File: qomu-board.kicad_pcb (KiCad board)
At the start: 4 copper layers, 13 x 9.4 mm, 55 parts, among them SW2 Captouch Pads, U1 LDO-X2SON-1.2V, U10 RGB-LED, U2 LDO-X2SON-3.3V, U3 LDO-X2SON-2.5V, U4 SPI Flash, U5 ICE40UP5K-UWG30, U7 Crystal Oscillator, U9 USB-B

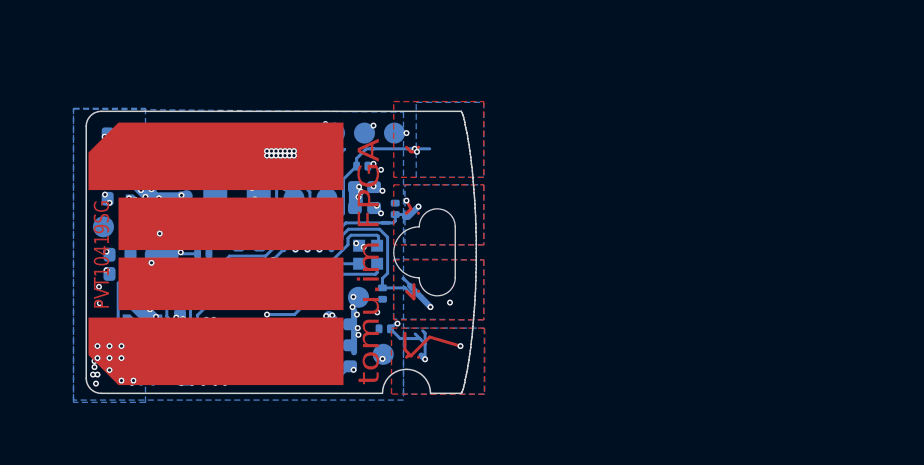
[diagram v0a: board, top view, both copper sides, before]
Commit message: Schematic/PCB cleanup
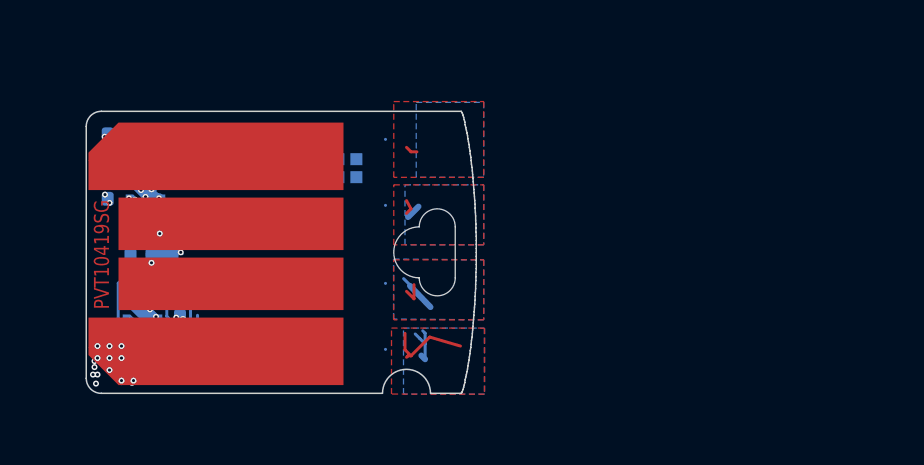
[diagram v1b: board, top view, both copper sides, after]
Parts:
- removed C10, C17, C24, C25, C5, C8: 0201, 1uF, 10V, X5R, 20%, qomu-board:C_0201_0603Metric
- removed C11, C20, C21, C23, C28, C4, C7: 0201, 100nF, 10V, X5R, 20%, qomu-board:C_0201_0603Metric
- removed C22: 0402, 10uF, 6.3V, X5R, 20%, qomu-board:C_0402_1005Metric
- removed D1, D2, D3, D4, D6: D5V0L1B2LP3-7, qomu-board:X1-DFN1006-2
- removed D5: VCUT05E1-SD0, qomu-board:TVS-11V
- removed R1, R5: 0201, 10k, 1/16W, qomu-board:R_0201_0603Metric
- removed R10: 0201, 100ohm, 1/16W, 1%, qomu-board:R_0201_0603Metric
- removed TP1, TP10, TP11, TP12, TP2, TP3, TP4, TP5, TP6, TP7, TP8, TP9: Testpoint, qomu-board:testpoint
- removed U4: SPI Flash, qomu-board:SON50P300X200X60-9N
- removed U5: ICE40UP5K-UWG30, qomu-board:iCE40UP5K-UWG30
- removed U7: Crystal Oscillator, qomu-board:XTAL-2520
- SW2: moved to B.Cu
- moved U10 2.97 mm to (25.7, 19.0), turned to 0 degrees
- moved SW2 1.13 mm to (27.0, 21.5), turned to 0 degrees
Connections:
- R11 pad 1: /ICE_USBN -> Net-(R11-Pad1)
- R12 pad 1: /ICE_USBP -> Net-(R12-Pad1)
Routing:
- net /SPI_MISO: track 29.6 -> 0.00 mm, vias 5 -> 0
- net /SPI_MOSI: track 27.6 -> 0.00 mm, vias 5 -> 0
- net /SPI_CS: track 22.7 -> 0.00 mm, vias 6 -> 0
- net /SPI_CLK: track 20.2 -> 0.00 mm, vias 3 -> 0
- net /CRESET: track 16.0 -> 0.00 mm, vias 4 -> 0
- net /SPI_IO2: track 15.1 -> 0.00 mm, vias 4 -> 0
- net +1V2: track 14.7 -> 1.24 mm, vias 18 -> 4
- net /SPI_IO3: track 9.91 -> 0.00 mm, vias 4 -> 0
- net /ICE_USBN: track 9.19 -> 0.00 mm
- net /ICE_USBP: track 9.01 -> 0.00 mm
- net +3V3: track 9.26 -> 0.86 mm, vias 44 -> 9
- net /TOUCH_1: track 13.0 -> 4.62 mm, vias 7 -> 0
- net +2V5: track 7.56 -> 0.02 mm, vias 10 -> 0
- net GND: track 20.1 -> 13.0 mm, vias 86 -> 25
- net /PU_CTRL_USBP: track 7.46 -> 0.74 mm, vias 2 -> 1
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- removed copper zone on In1.Cu, net +1V2
- removed copper zone on In2.Cu, net +1V2
- removed copper zone on In1.Cu, net +2V5
- removed copper zone on In1.Cu, net +3V3
- removed copper zone on In2.Cu, net +3V3
- removed copper zone on B.Cu, net +5V
- removed copper zone on In1.Cu, net +5V
- removed copper zone on In2.Cu, net +5V
- removed copper zone on In1.Cu, net /VCCPLL
- removed copper zone on B.Cu, net GND
- removed copper zone on In1.Cu, net GND
- removed copper zone on In2.Cu, net GND
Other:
- board text removed: "tomu.im FPGA"

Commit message: Added EOS-S3 and flash memory to schematics
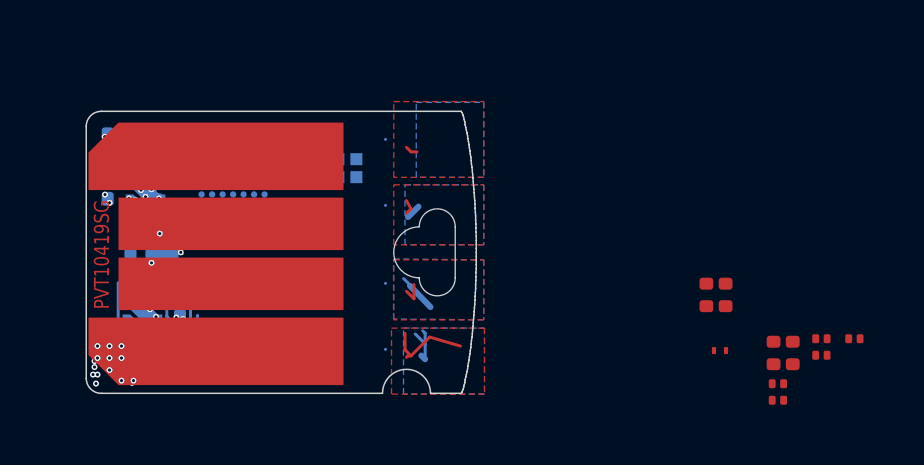
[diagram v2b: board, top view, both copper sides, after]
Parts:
- added C10: 1u/10V, qomu-board:C_0201_0603Metric, F.Cu at (40.3, 24.8)
- added C8: 1u/10V, qomu-board:C_0201_0603Metric, F.Cu at (40.3, 25.5)
- added D1: D5V0L1B2LP3-7, qomu-board:X1-DFN1006-2, F.Cu at (41.5, 24.7)
- added D2: D5V0L1B2LP3-7, qomu-board:X1-DFN1006-2, F.Cu at (40.1, 26.2)
- added D3: D5V0L1B2LP3-7, qomu-board:X1-DFN1006-2, F.Cu at (41.5, 25.2)
- added D4: D5V0L1B2LP3-7, qomu-board:X1-DFN1006-2, F.Cu at (40.1, 26.7)
- added D5: VCUT05E1-SD0, qomu-board:TVS-11V, F.Cu at (38.1, 25.1)
- added D6: D5V0L1B2LP3-7, qomu-board:X1-DFN1006-2, F.Cu at (42.6, 24.7)
- added IC1: EOS-S3, qomu-board:42-WLCSP, B.Cu at (21.9, 19.0)
- added R1: 10k, qomu-board:R_0201_0603Metric, F.Cu at (38.0, 23.6)
- added R2: 0R, qomu-board:R_0201_0603Metric, F.Cu at (38.0, 22.8)
- C1, C2, C3, C9: value 0201, 1uF, 10V, X5R, 20% -> 1u/10V
- R11, R12: value 0201, 22ohm, 1/16W, 1% -> 22R
- R9: value 0201, 1.5k, 1/16W, 1% -> 1k5
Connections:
- net +1V2 renamed /1V2_SYS
- net +3V3 renamed /3V3_SYS
- net +5V renamed /USB_VBUS
- U3 pad 1: +2V5 -> /2v5_SYS
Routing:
- net +5V: track 0.00 -> 0.47 mm, vias 0 -> 15
- net /USB_VBUS: track 5.57 -> 5.10 mm, vias 27 -> 12
- net /3V3_SYS: vias 9 -> 6
- net +3V3: vias 0 -> 3

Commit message: Added accelerometer, changed flash memory
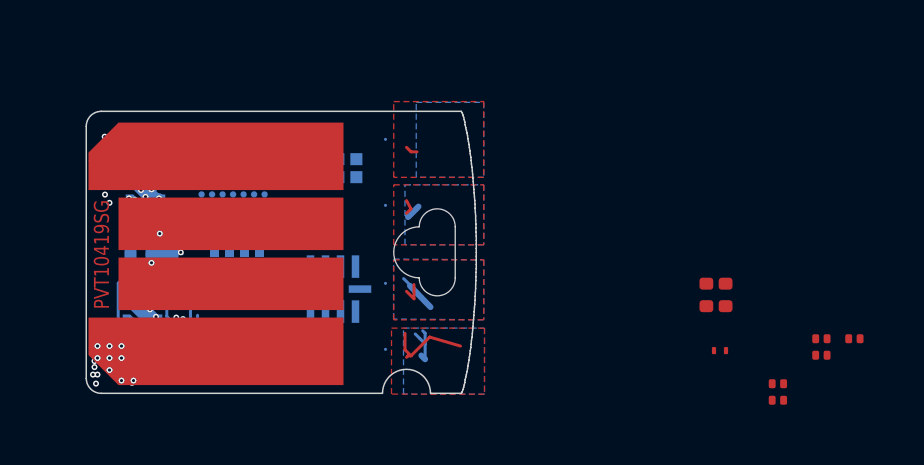
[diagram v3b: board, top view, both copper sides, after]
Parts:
- removed C1, C10, C2, C3, C8, C9: 1u/10V, qomu-board:C_0201_0603Metric
- added U4: GD25Q16CEIGR, antmicro-footprints:GD25Q16CEIGR, B.Cu at (22.1, 23.3)
- added U5: MC3635, antmicro-footprints:MC3635, B.Cu at (25.2, 22.8)

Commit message: Fixed missing library components, fixed MC3635 footprint
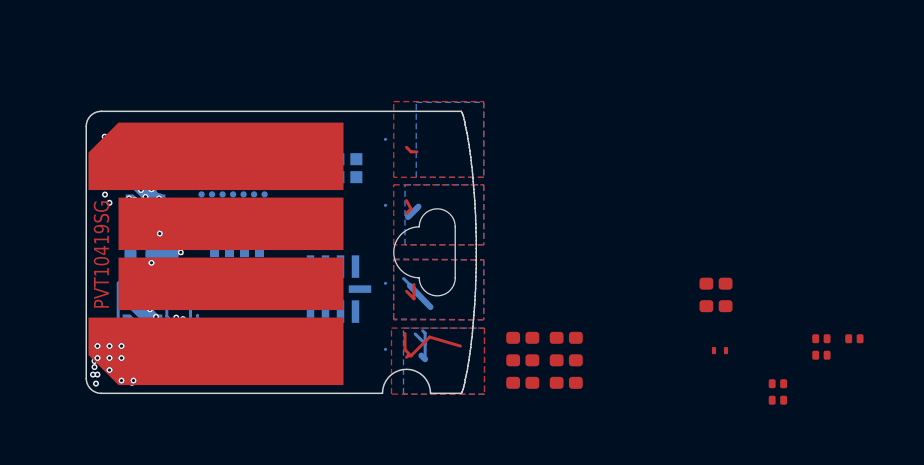
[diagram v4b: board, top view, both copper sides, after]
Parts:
- added C1: 1u/10V, qomu-board:C_0201_0603Metric, F.Cu at (31.6, 24.7)
- added C10: 1u/10V, qomu-board:C_0201_0603Metric, F.Cu at (31.6, 25.4)
- added C2: 1u/10V, qomu-board:C_0201_0603Metric, F.Cu at (33.0, 26.2)
- added C3: 1u/10V, qomu-board:C_0201_0603Metric, F.Cu at (33.0, 25.4)
- added C8: 1u/10V, qomu-board:C_0201_0603Metric, F.Cu at (31.6, 26.2)
- added C9: 1u/10V, qomu-board:C_0201_0603Metric, F.Cu at (33.0, 24.7)
- U4: footprint antmicro-footprints:GD25Q16CEIGR -> qomu-board:GD25Q16CEIGR

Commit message: Connected U4 and U5 to EOS S3
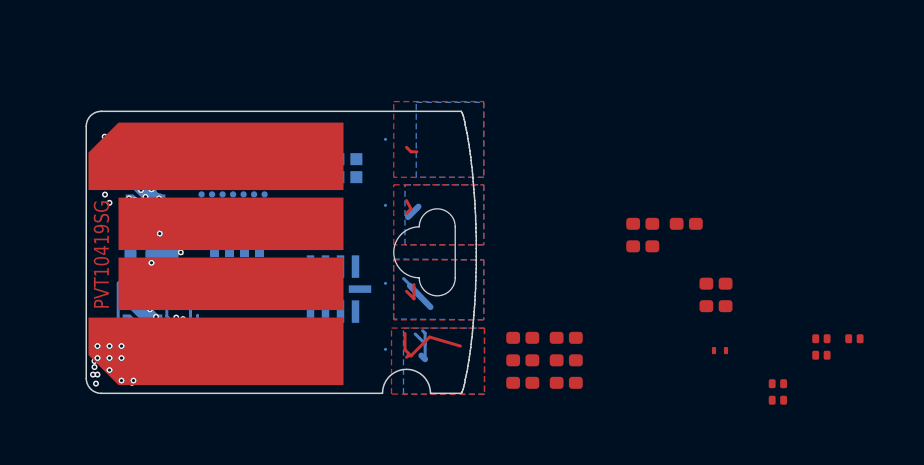
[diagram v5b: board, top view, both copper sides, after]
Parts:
- added C4: 100n, qomu-board:C_0201_0603Metric, F.Cu at (37.0, 20.9)
- added R3: 4k7, qomu-board:R_0201_0603Metric, F.Cu at (35.6, 20.9)
- added R4: 4k7, qomu-board:R_0201_0603Metric, F.Cu at (35.6, 21.6)
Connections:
- IC1 pad A7: Net-(IC1-PadA7) -> /I2C_SCL
- IC1 pad B7: Net-(IC1-PadB7) -> /I2C_SDA
- IC1 pad D5: Net-(IC1-PadD5) -> /SPI_SCLK
- IC1 pad E6: Net-(IC1-PadE6) -> /SPI_MOSI
- IC1 pad F5: Net-(IC1-PadF5) -> /SPI_MISO
- U4 pad 2: Net-(U4-Pad2) -> /SPI_MISO
- U4 pad 4: Net-(U4-Pad4) -> GND
- U4 pad 5: Net-(U4-Pad5) -> /SPI_MOSI
- U4 pad 6: Net-(U4-Pad6) -> /SPI_SCLK
- U4 pad 8: Net-(U4-Pad8) -> /3V3_SYS
- U5 pad 1: Net-(U5-Pad1) -> GND
- U5 pad 10: Net-(U5-Pad10) -> /I2C_SCL
- U5 pad 2: Net-(U5-Pad2) -> /I2C_SDA
- U5 pad 4: Net-(U5-Pad4) -> GND
- U5 pad 6: Net-(U5-Pad6) -> /3V3_SYS
- U5 pad 7: Net-(U5-Pad7) -> /3V3_SYS
- U5 pad 8: Net-(U5-Pad8) -> GND
- U5 pad 9: Net-(U5-Pad9) -> GND

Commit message: Added plastic case outline to PCB, defined initial component placement
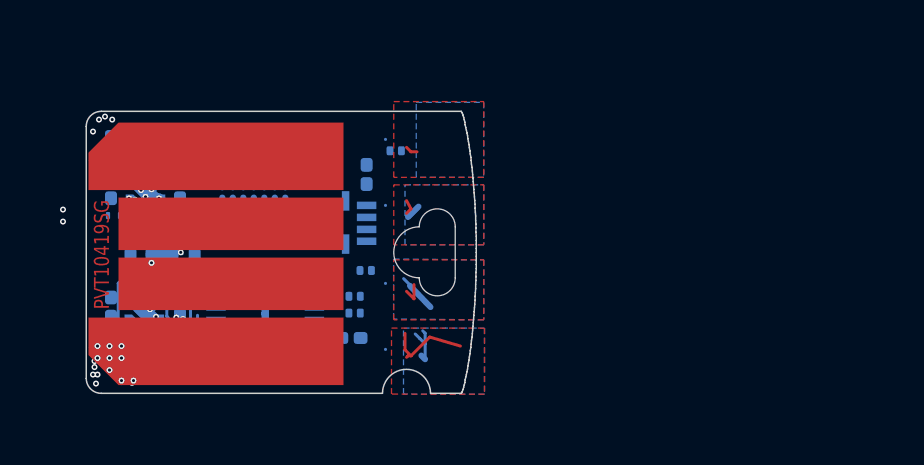
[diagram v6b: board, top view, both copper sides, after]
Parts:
- added C5: 100n, qomu-board:C_0201_0603Metric, B.Cu at (25.9, 24.7)
- C1, C10, C2, C3, C4, C8, C9, D1, D2, D3, D4, D5, D6, R1, R2, R3, R4: moved to B.Cu
- moved D6 23.3 mm to (19.6, 21.0)
- moved D5 20.7 mm to (17.9, 20.6)
- moved R1 17.4 mm to (20.6, 22.2), turned to 270 degrees
- moved C2 16.5 mm to (17.9, 19.7), turned to 270 degrees
- moved D3 15.7 mm to (27.3, 18.4), turned to 180 degrees
- moved D1 15.6 mm to (26.0, 23.8), turned to 180 degrees
- moved R2 15.4 mm to (23.2, 18.7)
- moved C3 15.3 mm to (17.9, 23.6), turned to 90 degrees
- moved C1 15.1 mm to (17.9, 18.3), turned to 270 degrees
- moved D2 14.4 mm to (26.0, 23.3), turned to 180 degrees
- moved D4 14.4 mm to (26.3, 22.4), turned to 180 degrees
- moved C8 13.9 mm to (20.2, 18.2), turned to 270 degrees
- moved R4 13.6 mm to (22.0, 22.3), turned to 180 degrees
- moved C9 12.9 mm to (20.1, 23.6), turned to 270 degrees
- moved C10 12.8 mm to (20.1, 19.7), turned to 270 degrees
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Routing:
- net /EOS_VDD: vias 0 -> 1
- net +3V3: vias 3 -> 2

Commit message: Updated component placement
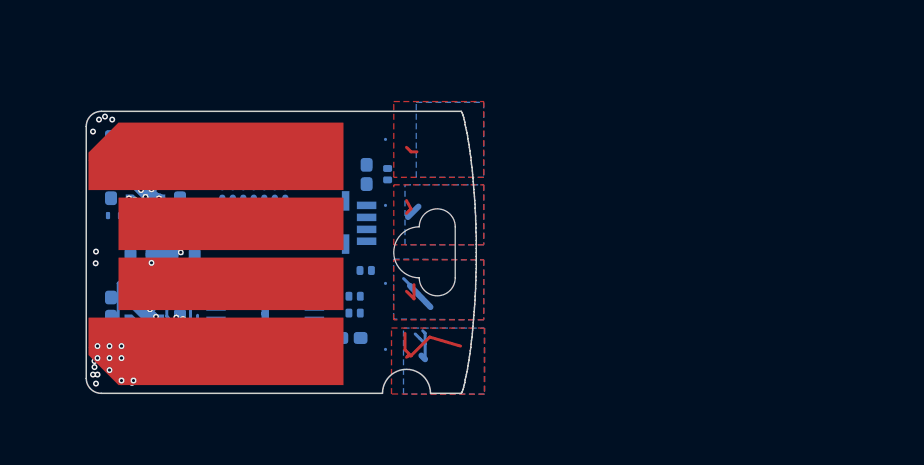
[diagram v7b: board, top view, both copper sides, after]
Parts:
- moved D3 0.83 mm to (27.1, 19.2), turned to 90 degrees
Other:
- board text removed: "PVT10419SG"
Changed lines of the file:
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@@
   (general
     (thickness 0.6)
-    (drawings 177)
+    (drawings 176)
     (tracks 199)
     (zones 0)
@@
     (37 F.SilkS user hide)
     (38 B.Mask user)
-    (39 F.Mask user hide)
+    (39 F.Mask user)
     (40 Dwgs.User user hide)
     (41 Cmts.User user)
@@
     (at 25.92 20.805)
     (attr smd)
-    (fp_text reference U5 (at 0 1.975) (layer B.SilkS)
+    (fp_text reference U5 (at -1.33 -3.97) (layer B.SilkS) hide
       (effects (font (size 1 1) (thickness 0.15)) (justify mirror))
     )
@@
     (at 22.99 23.845)
     (attr smd)
-    (fp_text reference U4 (at 0 2.175) (layer B.SilkS)
+    (fp_text reference U4 (at -1.2 3.83) (layer B.SilkS) hide
       (effects (font (size 1 1) (thickness 0.15)) (justify mirror))
     )
@@
     (at 22.61 20.505)
     (attr smd)
-    (fp_text reference IC1 (at 0 2.211) (layer B.SilkS)
+    (fp_text reference IC1 (at -0.2 -2.83) (layer B.SilkS) hide
       (effects (font (size 1 1) (thickness 0.15)) (justify mirror))
     )
@@
   )
   (module qomu-board:X1-DFN1006-2 (layer B.Cu)
-    (at 27.34 18.415 180)
+    (at 27.07 19.195 90)
     (descr https://datasheet.lcsc.com/szlcsc/Diodes-Incorporated-D5V0L1B2LP3-7_C282418.pdf)
     (tags ESD)
     (attr smd)
-    (fp_text reference D3 (at 1.9 0 180) (layer B.SilkS) hide
+    (fp_text reference D3 (at 1.9 0 90) (layer B.SilkS) hide
       (effects (font (size 0.5 0.5) (thickness 0.125)) (justify mirror))
     )
-    (fp_text value D5V0L1B2LP3-7 (at -0.005 0.275 180) (layer B.Fab)
+    (fp_text value D5V0L1B2LP3-7 (at -0.005 0.275 90) (layer B.Fab)
       (effects (font (size 0.1 0.1) (thickness 0.025)) (justify mirror))
     )
@@
     (fp_line (start 0.525 0.25) (end 0.525 -0.25) (layer B.CrtYd) (width 0.05))
     (fp_line (start -0.525 0.25) (end 0.525 0.25) (layer B.CrtYd) (width 0.05))
-    (fp_text user %R (at 0 0) (layer B.Fab)
+    (fp_text user %R (at 0 0 -90) (layer B.Fab)
       (effects (font (size 0.15 0.15) (thickness 0.025)) (justify mirror))
     )
@@
     (fp_line (start 0.31 -0.16) (end -0.31 -0.16) (layer B.Fab) (width 0.1))
     (fp_line (start -0.31 -0.16) (end -0.31 0.16) (layer B.Fab) (width 0.1))
-    (pad 2 smd roundrect (at 0.19 0 180) (size 0.23 0.3) (layers B.Cu B.Paste B.Mask) (roundrect_rratio 0.25)
-      (net 1 GND))
-    (pad 1 smd roundrect (at -0.19 0 180) (size 0.23 0.3) (layers B.Cu B.Paste B.Mask) (roundrect_rratio 0.25)
+    (pad 2 smd roundrect (at 0.19 0 90) (size 0.23 0.3) (layers B.Cu B.Paste B.Mask) (roundrect_rratio 0.25)
+      (net 1 GND))
+    (pad 1 smd roundrect (at -0.19 0 90) (size 0.23 0.3) (layers B.Cu B.Paste B.Mask) (roundrect_rratio 0.25)
       (net 5 /TOUCH_4))
     (model ${KISYS3DMOD}/Inductor_SMD.3dshapes/L_0201_0603Metric.wrl
@@
     (solder_mask_margin 0.000001)
     (attr virtual)
-    (fp_text reference U9 (at 1.25 1.65) (layer Cmts.User)
+    (fp_text reference U9 (at 1.25 1.65) (layer Cmts.User) hide
       (effects (font (size 1 1) (thickness 0.15)))
     )
@@
   (gr_text "PCB Soldermask: Dark Blue\nPCB Thickness: 0.6mm\nHard gold plating on fingers, side\nENIG on other surfaces" (at 16.55 37.45) (layer Eco1.User)
     (effects (font (size 2.5 2.5) (thickness 0.3)) (justify left))
-  )
-  (gr_text PVT10419SG (at 17.55 21.875 90) (layer F.Cu)
-    (effects (font (size 0.5 0.41) (thickness 0.1025)))
   )
   (gr_arc (start 28.725 22.65) (end 28.125 22.65) (angle -180) (layer Edge.Cuts) (width 0.01))
@@
   (via micro (at 20.4 22.6) (size 0.2) (drill 0.1) (layers In2.Cu B.Cu) (net 2) (status 30))
   (via blind (at 20.225 22.775) (size 0.5) (drill 0.2) (layers In1.Cu In2.Cu) (net 2))
-  (via micro (at 20.45 22.475) (size 0.2) (drill 0.1) (layers In2.Cu B.Cu) (net 48) (status 30))
   (segment (start 18.2 25.55) (end 18.2 25.5) (width 0.1) (layer In2.Cu) (net 3))
   (segment (start 18.2 25.5) (end 18 25.7) (width 0.1) (layer In2.Cu) (net 3))
@@
   (segment (start 19.2 21.88) (end 19.9 21.88) (width 0.4) (layer B.Cu) (net 12) (status 30))
   (via blind (at 19.625 21.65) (size 0.5) (drill 0.2) (layers In1.Cu In2.Cu) (net 12))
-  (via micro (at 16.25 20.775) (size 0.2) (drill 0.1) (layers F.Cu In1.Cu) (net 12))
+  (via micro (at 17.34 22.165) (size 0.2) (drill 0.1) (layers F.Cu In1.Cu) (net 12))
   (segment (start 19.475 21.5) (end 19.625 21.65) (width 0.1) (layer In1.Cu) (net 12))
   (segment (start 19.475 21.175) (end 19.475 21.5) (width 0.1) (layer In1.Cu) (net 12))
@@
   (segment (start 18.5 21.5) (end 18.5 21.88) (width 0.1) (layer B.Cu) (net 13))
   (segment (start 19.025 20.975) (end 18.5 21.5) (width 0.1) (layer B.Cu) (net 13))
-  (via micro (at 16.25 20.375) (size 0.2) (drill 0.1) (layers In2.Cu B.Cu) (net 13))
+  (via micro (at 17.35 21.775) (size 0.2) (drill 0.1) (layers In2.Cu B.Cu) (net 13))
   (segment (start 19 21) (end 19.025 20.975) (width 0.1) (layer B.Cu) (net 13))
   (segment (start 19.05 21.175) (end 19 21) (width 0.1) (layer B.Cu) (net 13))
@@
   (segment (start 18.35 23.85) (end 18.58 23.525) (width 0.4) (layer In1.Cu) (net 47))
   (segment (start 18.58 23.525) (end 18.58 23.509002) (width 0.4) (layer In1.Cu) (net 47))
+  (via micro (at 20.45 22.475) (size 0.2) (drill 0.1) (layers In2.Cu B.Cu) (net 48) (status 30))
   (zone (net 5) (net_name /TOUCH_4) (layer B.Cu) (hatch edge 0.508)
     (priority 2)

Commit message: Connected missing nets, schematic cleanup
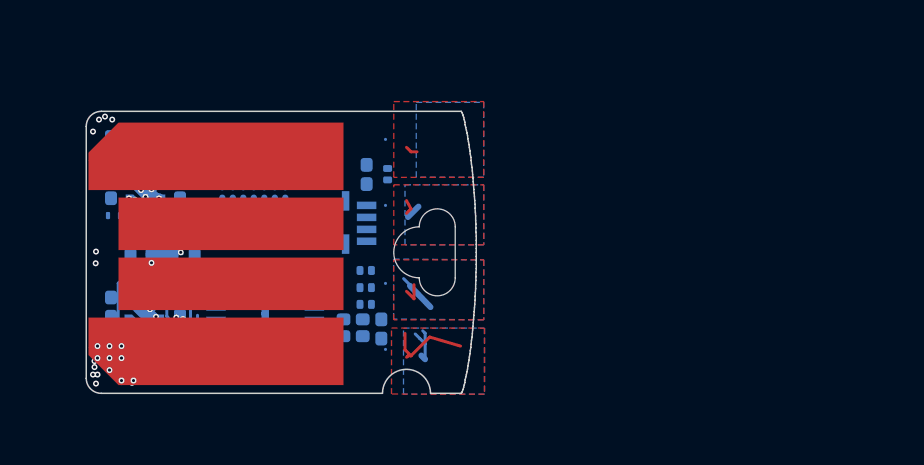
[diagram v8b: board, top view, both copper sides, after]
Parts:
- added R5: 10k, qomu-board:R_0201_0603Metric, B.Cu at (26.9, 24.4)
- added R6: 10k, qomu-board:R_0201_0603Metric, B.Cu at (20.2, 25.1)
- added R7: 10k, qomu-board:R_0201_0603Metric, B.Cu at (25.9, 24.0)
- U5: footprint antmicro-footprints:MC3635 -> qomu-board:MC3635
- moved D1 0.47 mm to (26.3, 23.5)
- moved D2 0.47 mm to (26.3, 23.0)
- moved C5 0.09 mm to (25.9, 24.6)
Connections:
- IC1 pad E2: Net-(IC1-PadE2) -> /PU_CTRL_USBP
- IC1 pad E3: Net-(IC1-PadE3) -> /PU_CTRL_USBP
- IC1 pad F3: Net-(IC1-PadF3) -> /R_USB_N
- IC1 pad F6: Net-(IC1-PadF6) -> /SPI_SS
- R11 pad 1: Net-(R11-Pad1) -> /R_USB_N
- R12 pad 1: Net-(R12-Pad1) -> /PU_CTRL_USBP
- U4 pad 1: Net-(U4-Pad1) -> /SPI_SS
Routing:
- net Net-(R11-Pad1): track 5.04 -> 0.00 mm
- net /R_USB_N: track 0.00 -> 5.04 mm
- net Net-(R12-Pad1): track 4.29 -> 0.00 mm
- net /PU_CTRL_USBP: track 0.74 -> 5.03 mm
- net GND: vias 25 -> 26
- net +5V: vias 15 -> 14
